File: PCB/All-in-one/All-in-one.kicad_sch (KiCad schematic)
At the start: 62 parts, among them J1 HIGH VOLTAGE, J2 Micro_SD_Card_Det, J3 USB_C_Receptacle_USB2.0, J4 I2C_EXT, J5 GPIO, J6 SWD, J7 Conn_01x02, J8 Conn_01x02, J9 UART_EXT, Q1 AO3401A, SW1 SW_Push, SW2 BOOT, U1 TPMP1470, U2 STM32F401CDUx, U3 BMP280, U4 MPU-6050, U5 USBLC6-2P6, Y1 25MHz 12pF

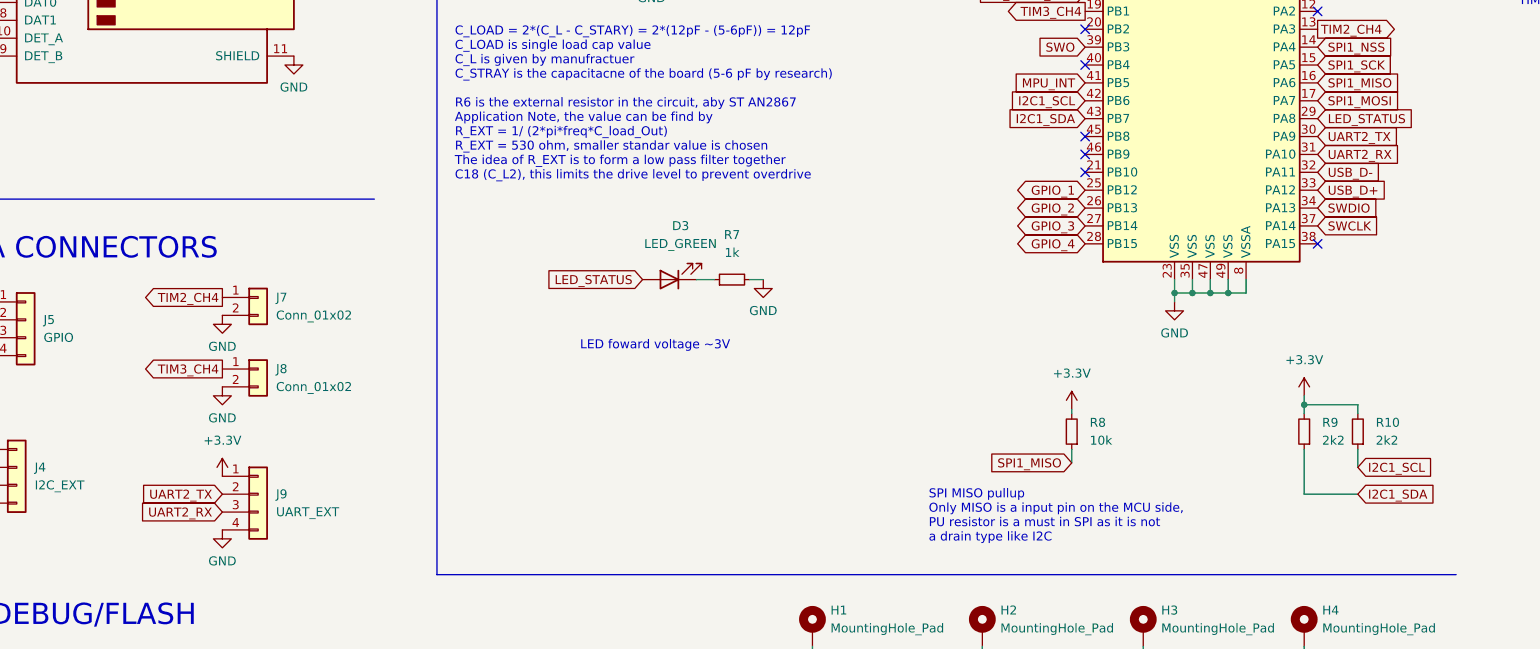
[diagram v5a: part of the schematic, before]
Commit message: Updated CubeIDE Code and Reviewed All-in-one X01 PCB - updated PCB labelling (UART_1 is mis-labelled as UART_2 on both .sch   and PCB) - Tried STM32 programming with simple PWM code
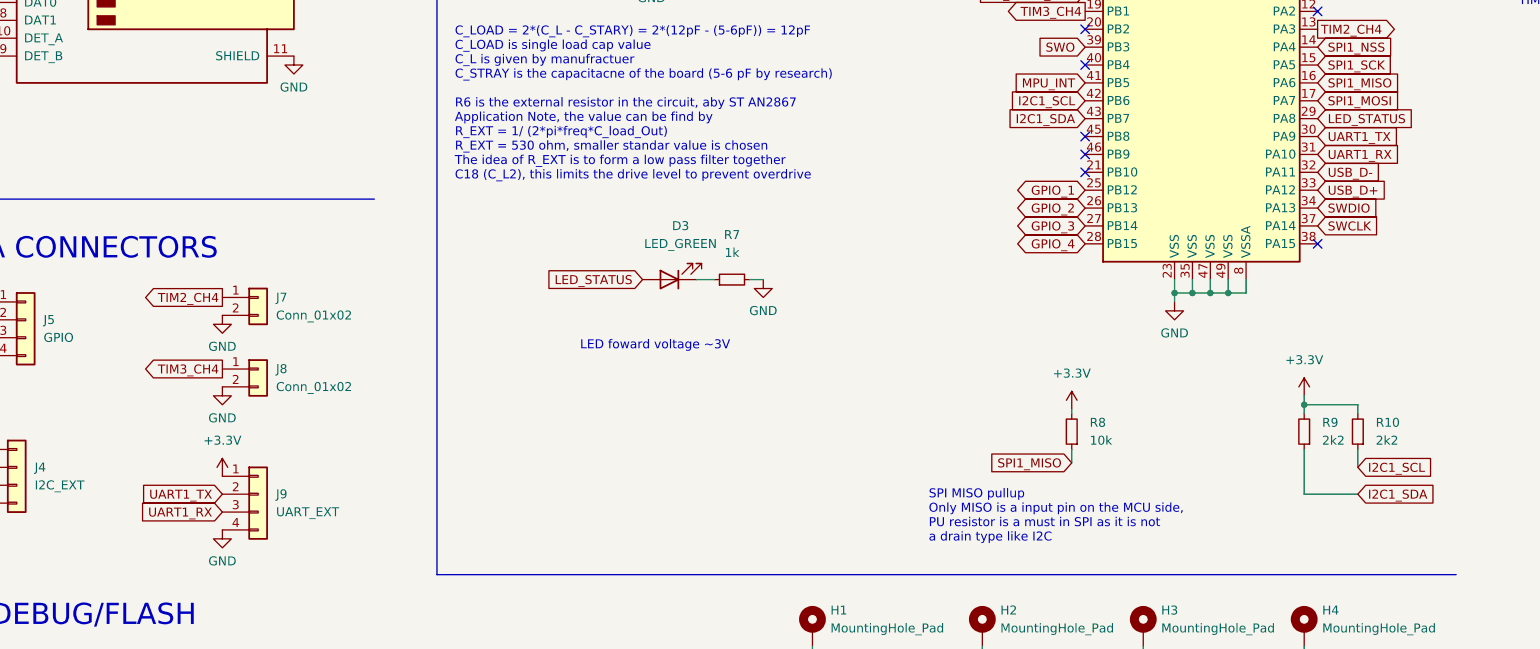
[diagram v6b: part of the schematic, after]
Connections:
- net UART2_RX renamed UART1_RX
- net UART2_TX renamed UART1_TX
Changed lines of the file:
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@@
     )
   )
-  (global_label "UART2_RX" (shape input) (at 398.145 154.94 0) (fields_autoplaced)
+  (global_label "UART1_RX" (shape input) (at 398.145 154.94 0) (fields_autoplaced)
     (effects (font (size 1.27 1.27)) (justify left))
     (property "Intersheet References" "${INTERSHEET_REFS}" (id 0) (at 409.8714 154.8606 0)
@@
     )
   )
-  (global_label "UART2_RX" (shape input) (at 242.57 205.74 180) (fields_autoplaced)
+  (global_label "UART1_RX" (shape input) (at 242.57 205.74 180) (fields_autoplaced)
     (effects (font (size 1.27 1.27)) (justify right))
     (property "Intersheet References" "${INTERSHEET_REFS}" (id 0) (at 230.8436 205.8194 0)
@@
     )
   )
-  (global_label "UART2_TX" (shape input) (at 242.57 203.2 180) (fields_autoplaced)
+  (global_label "UART1_TX" (shape input) (at 242.57 203.2 180) (fields_autoplaced)
     (effects (font (size 1.27 1.27)) (justify right))
     (property "Intersheet References" "${INTERSHEET_REFS}" (id 0) (at 231.1459 203.2794 0)
@@
     )
   )
-  (global_label "UART2_TX" (shape input) (at 398.145 152.4 0) (fields_autoplaced)
+  (global_label "UART1_TX" (shape input) (at 398.145 152.4 0) (fields_autoplaced)
     (effects (font (size 1.27 1.27)) (justify left))
     (property "Intersheet References" "${INTERSHEET_REFS}" (id 0) (at 409.5691 152.3206 0)
